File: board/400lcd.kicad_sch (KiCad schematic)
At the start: 1 part, among them J102 Conn_02x16_Top_Bottom

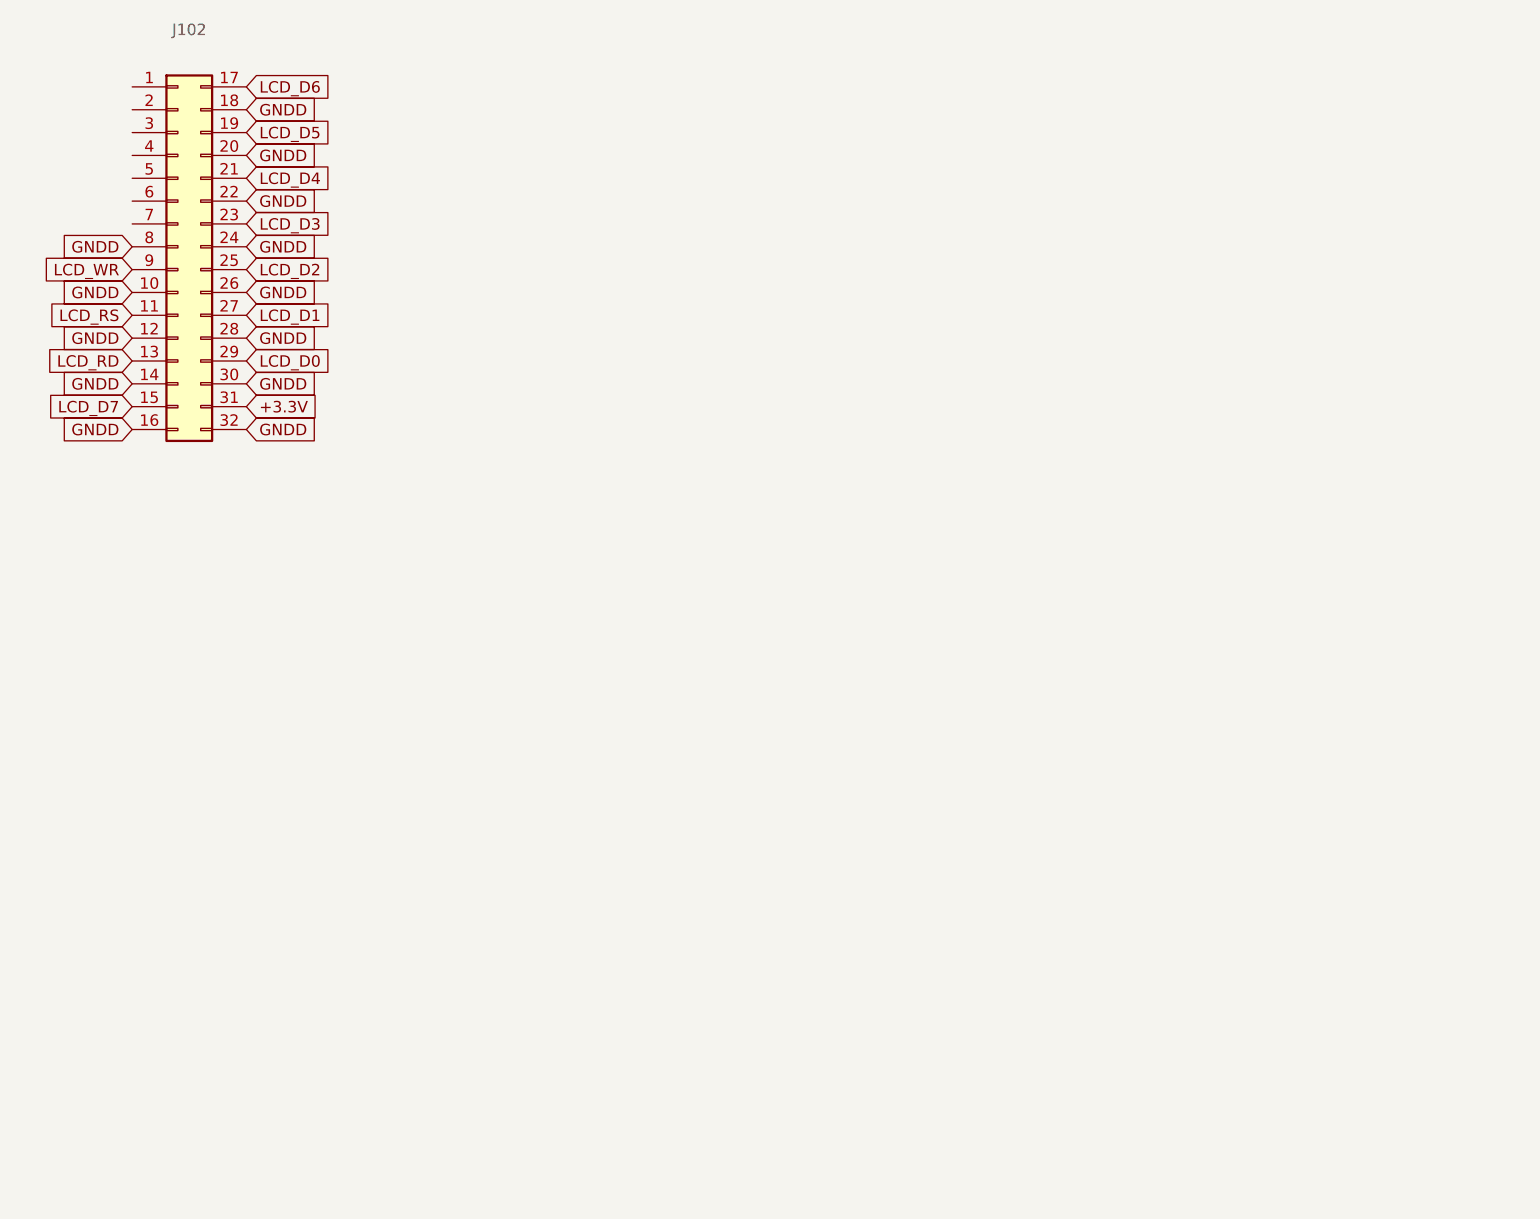
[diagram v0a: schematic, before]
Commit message: Added stl and skp files for 3D printing, changed ground planes and net names, exported schematics as pdf
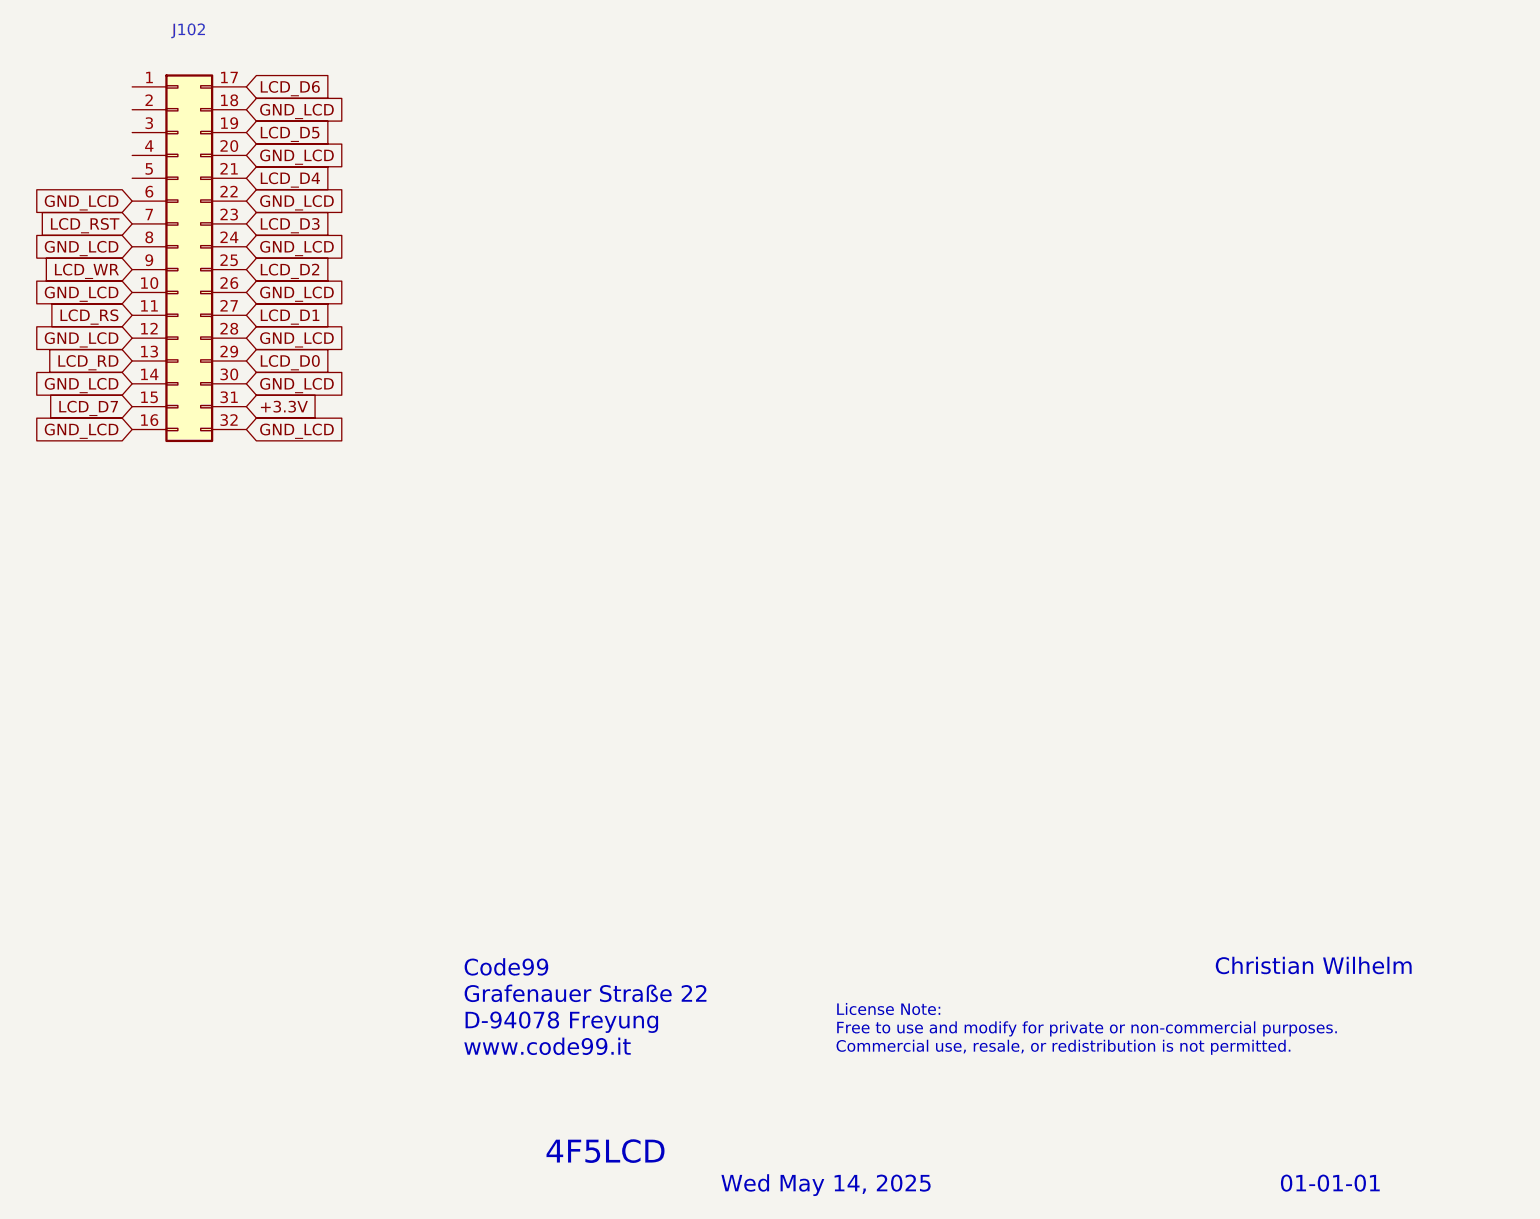
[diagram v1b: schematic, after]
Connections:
- net GNDD is gone; now on net GND_LCD: J102.10 (Pin_10), J102.12 (Pin_12), J102.14 (Pin_14), J102.16 (Pin_16), J102.18 (Pin_18), J102.20 (Pin_20), J102.22 (Pin_22), J102.24 (Pin_24), J102.26 (Pin_26), J102.28 (Pin_28), J102.30 (Pin_30), J102.32 (Pin_32), J102.8 (Pin_8)
- net GND_LCD: now reaches J102.6 (Pin_6)
- net LCD_RST: now reaches J102.7 (Pin_7)
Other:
- note added: "01-01-01"
- note added: "4F5LCD"
- note added: "Christian Wilhelm"
- note added: "Code99 Grafenauer Straße 22 D-94078 Freyung www.code99.it"
- note added: "License Note: Free to use and modify for private or non-commercial purposes. Commercial use, resale, or redistribution is not permitted."
- note added: "Wed May 14, 2025"
